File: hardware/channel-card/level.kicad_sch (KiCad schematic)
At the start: 63 parts, among them SW201 MUTE (latching), SW202 DUCK (latching), U201 SSI2162, U202 NE5532, U203 NE5532, U204 OPA2171, U205 TL072, U206 DG413DY

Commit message: Channel card: fee-free TL072CDT, 78L05G-AB3-R, BZT52C6V2, UNI-ROYAL resistors (decision 137)
SX-IC-007 TL072 -> ST TL072CDT (LCSC C6961, basic), SX-IC-012 78L05 -> UTC
78L05G-AB3-R (C71136, basic; pins 1 O 2 G 3 I, not the -AB3-C-R variant),
SX-D-001 -> hongjiacheng BZT52C6V2 (C19077403, preferred), SX-R-011/036/042
-> UNI-ROYAL 0805W8F (preferred). Datasheet facts and RoHS sources in
parts.csv. Filter, level, meter and chain sheets rebuilt: netlists match,
ERC 0/0. costs.py extended: 82 -> 80 fee types. Master STATUS notes that
its TL072 symbols still need the ST fields.

Co-Authored-By: Claude Opus 5.5 <noreply@anthropic.com>
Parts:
- U205: MPN (none) -> TL072CDT; Manufacturer Texas Instruments -> STMicroelectronics; Supplier (none) -> LCSC; SupplierPN (none) -> C6961

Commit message: Channel card: cost levers (decisions 139-143)
- U303 DG412 -> DG413, SC send on the NC section (139)
- All values E24 with JLCPCB fee-free parts; E24 pairs for V/oct
  and fader law, meter ladder re-fitted (140)
- Filter temperature compensation to the backlog (141)
- MUTE/DUCK switched by the buttons' spare pole, U206 DG413 removed;
  100k hold resistors, no dependence on contact sequence (142)
- TL072 difference receiver with 10k 0.1 % instead of the AD8273 (143)
- Trimmers from Mouser, CUTOFF pot from Tayda A-4730
- Breadboard tests 11 (X5R coupling caps) and 12 (fixed V/oct)
- costs.py estimate, 4 channels: EUR 1,035 -> 946

Co-Authored-By: Claude Opus 5.5 <noreply@anthropic.com>
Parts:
- removed C235, C236: 100n, Capacitor_SMD:C_0805_2012Metric, symbol Device:C
- removed U206: DG413DY, Package_SO:SOIC-16_3.9x9.9mm_P1.27mm, symbol Analog_Switch:DG413xY
- added R223: 13k, Resistor_SMD:R_0805_2012Metric, symbol Device:R
- added R224: 150k, Resistor_SMD:R_0805_2012Metric, symbol Device:R
- added R225: 24k, Resistor_SMD:R_0805_2012Metric, symbol Device:R
- R207: value 113k -> 100k; ProjectPN SX-R-023 -> SX-R-007
- R208: value 453k -> 300k; ProjectPN SX-R-024 -> SX-R-096
- R210: value 221k -> 220k; ProjectPN SX-R-025 -> SX-R-103
- R211: value 63k4 -> 62k; ProjectPN SX-R-026 -> SX-R-102
- R213: value 124k -> 100k; ProjectPN SX-R-027 -> SX-R-007
- R214: value 8k66 -> 9k1; ProjectPN SX-R-014 -> SX-R-095
- R216: value 33k2 -> 33k; ProjectPN SX-R-028 -> SX-R-006
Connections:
- net +15V: now also R225.1; no longer R213.1
- net -15V: now also SW201.3 (C)
- net AGND: now also R220.1, R222.1
- net DUCK_V: now also R222.2, SW202.2 (B)
- net MUTE_V: now also R220.2, SW201.2 (B)
- net PGND: no longer R220.1, R222.1
- net SC_ENV: now also SW202.3 (C)
- net at C224.1, R211.2, R214.2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: now also R223.2, R224.2; no longer R207.2, R208.2
- removed net +5V: SW201.2 (B), SW202.2 (B)
- removed net DUCK_CTRL: R222.2, SW202.3 (C)
- removed net MUTE_CTRL: R220.2, SW201.3 (C)
- new net: R207.2, R223.1
- new net: R208.2, R224.1
- new net: R213.1, R225.2

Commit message: Channel card: R217 30k (decision 153), SSI2144/SSI2162 hand-soldered on the prototype (decision 155)
Level sheet: R217 30k1 -> 30k (SX-R-050, basic); ducking -10.10 dB per -1 V
in simulation/level. U101/U102 SSI2144 and U201 SSI2162 carry Assembly =
"hand (decision 155)": 38 -> 36 fee types, 4/8/16 channels EUR 788/1,069/1,665.
Bipolar 10 uF caps stay consigned until breadboard test 11. Netlists match,
ERC 0/0.

Co-Authored-By: Claude Opus 5.5 <noreply@anthropic.com>
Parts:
- R217: value 30k1 -> 30k; Note SC_ENV into the virtual earth: 0.332 V/V, 10 dB of ducking 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 -> SC_ENV into the virtual earth: 0.333 V/V, 10 dB of ducking 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; ProjectPN SX-R-087 -> SX-R-050
- U201: Assembly (none) -> hand (decision 155)

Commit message: Buttons: SX-SW-001 is the latching GPBS850L, not the momentary GPBS850N
Electrokit 41012905 (on-on, latching) links the GPBS850N datasheet, which
is the momentary twin (Electrokit 41015527, Mouser "Non-Latching ON-(ON)");
the MPN was copied from that file. The latching part is CW GPBS850L
(datasheet Rev 2, 2014: same body, pin grid and pressed = 2-3, 5-6 contacts;
plunger 4.0 mm instead of 3.8).

MPN and footprint name corrected on all 17 button symbols, the generator
scripts and the input reference; parts.csv gets the GPBS850L datasheet and
RoHS source (Mouser 629-GPBS-850L, DigiKey CW179-ND); prices.csv gets the
Electrokit price (6.48 SEK ex VAT at 25+). Erratum on decision 75, checklist
item for the delivered switches and cap sizing, correction notes in the
RoHS audit and the cost review. No wiring change; ERC 0/0 on both cards.
Estimate €769 / €1,037 / €1,609 for 4 / 8 / 16 channels.

Co-Authored-By: Claude Opus 5.5 <noreply@anthropic.com>
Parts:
- SW201, SW202: footprint syntsamix:SW_Latching_8.5x8.5mm_CW_GPBS850N -> syntsamix:SW_Latching_8.5x8.5mm_CW_GPBS850L; MPN GPBS850N -> GPBS850L
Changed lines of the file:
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@@
 			)
 		)
-		(property "Footprint" "syntsamix:SW_Latching_8.5x8.5mm_CW_GPBS850N"
+		(property "Footprint" "syntsamix:SW_Latching_8.5x8.5mm_CW_GPBS850L"
 			(at 60.96 358.14 0)
 			(hide yes)
@@
 			)
 		)
-		(property "MPN" "GPBS850N"
+		(property "MPN" "GPBS850L"
 			(at 60.96 358.14 0)
 			(hide yes)
@@
 			)
 		)
-		(property "Footprint" "syntsamix:SW_Latching_8.5x8.5mm_CW_GPBS850N"
+		(property "Footprint" "syntsamix:SW_Latching_8.5x8.5mm_CW_GPBS850L"
 			(at 157.48 358.14 0)
 			(hide yes)
@@
 			)
 		)
-		(property "MPN" "GPBS850N"
+		(property "MPN" "GPBS850L"
 			(at 157.48 358.14 0)
 			(hide yes)

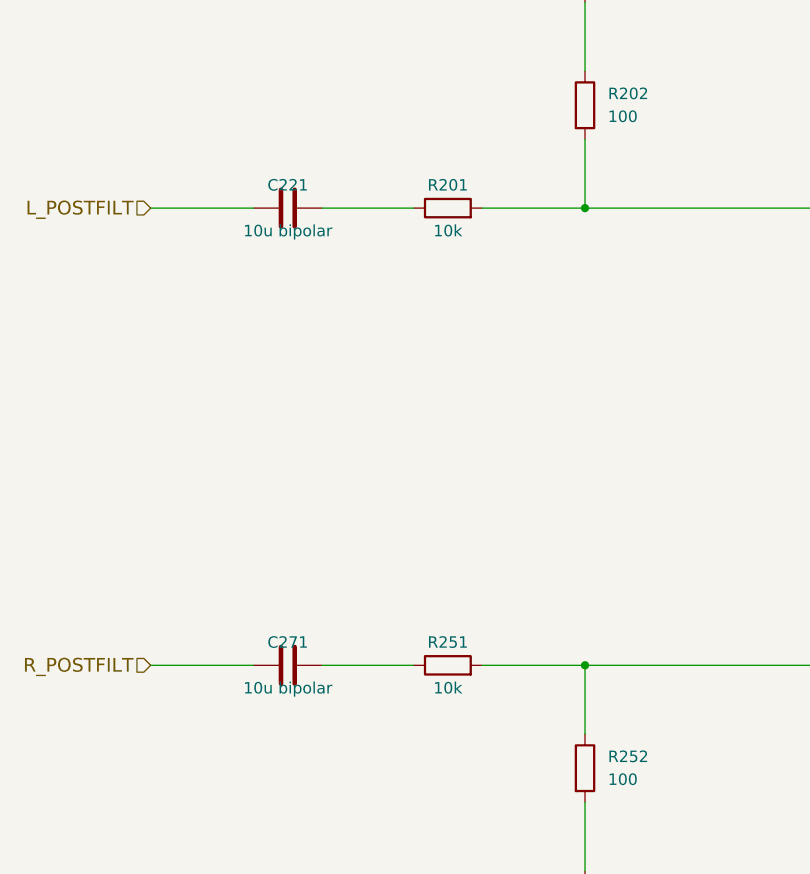
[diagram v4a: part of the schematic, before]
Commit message: Channel card: coupling capacitors as back-to-back ROQANG pairs (decision 161)
Each 10 uF bipolar coupling capacitor (Panasonic EEE-1VA100NP, out of stock
at LCSC and consigned) becomes two ROQANG RVT1V100M0505 10 uF 35 V (SX-C-024,
already on the card) in series, negative to negative: C5+C21, C6+C22,
C101+C108, C151+C158, C107+C109, C157+C159, C221+C235, C271+C285. No new fee
type, nothing on the channel card consigned. Netlists match (input 48,
filter 85, level 43 nets), ERC 0/0. Breadboard test 11 now checks the pair;
the X5R option is dropped. Estimate EUR 778 -> 768 for 4 channels; the
master follows in its own session.

Co-Authored-By: Claude Opus 5.5 <noreply@anthropic.com>
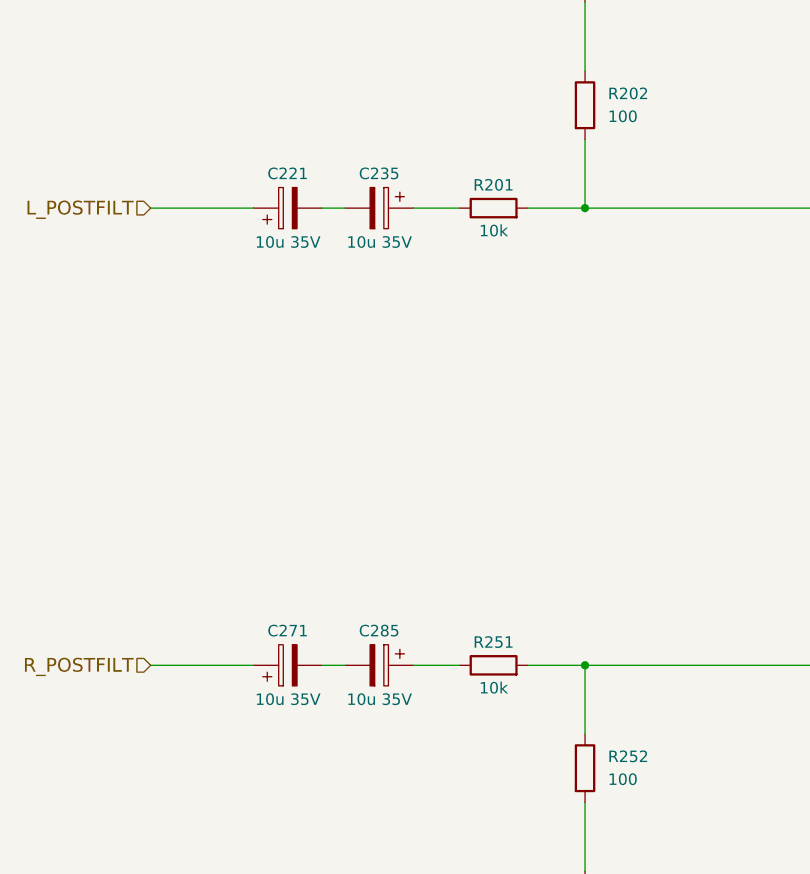
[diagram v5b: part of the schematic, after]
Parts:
- removed C221, C271: 10u bipolar, Capacitor_SMD:C_Elec_6.3x5.4, symbol Device:C
- added C221, C235, C271, C285: 10u 35V, Capacitor_SMD:CP_Elec_5x5.4, symbol Device:C_Polarized
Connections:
- net L_POSTFILT: now also C221.1
- net R_POSTFILT: now also C271.1
- net at R201.1: now also C235.1
- net at R251.1: now also C285.1
- new net: C271.2, C285.2
- new net: C221.2, C235.2
